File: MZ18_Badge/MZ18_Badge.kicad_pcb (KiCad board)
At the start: 2 copper layers, 76.5 x 89.8 mm, 57 parts, among them CN1 USBMOLEX, IC1 CMWX1ZZABZ-078, IC2 MCP73831_OT, J1 Conn_01x04, J2 Conn_01x04, J3 Conn_01x02, J4 Conn_01x12, J5 U.FL, J6 Conn_01x17, M1 SPI_FLASH-X25XXSMD, Q1 MMBT2222, Q2 MMBT2222, SW1 SW_Push, SW2 SW_Push, U1 ATSAMD21G-A, U2 SPX3819M5-L-3-3, U3 ESP32-WROOM, U4 CP2104, X1 XTALNX5032

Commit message: Desig (almost) done
Via stiching not yet done
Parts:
- removed J4: Conn_01x12, Socket_Strips:Socket_Strip_Angled_2x06_Pitch2.54mm
- removed J6: Conn_01x17, Socket_Strips:Socket_Strip_Angled_1x17_Pitch2.54mm
- added C17: 1u, Capacitors_SMD:C_0603_HandSoldering, B.Cu at (182.0, 130.0)
- added C18: 1u, Capacitors_SMD:C_0603_HandSoldering, B.Cu at (182.0, 127.0)
- added L1: INDUCTOR, Inductors_SMD:L_0603_HandSoldering, B.Cu at (179.0, 128.5)
- added R15: 100k, Resistors_SMD:R_0603_HandSoldering, B.Cu at (162.7, 121.6)
- added R16: 100k, Resistors_SMD:R_0603_HandSoldering, B.Cu at (164.3, 121.6)
- added R17: 0, Resistors_SMD:R_0603_HandSoldering, B.Cu at (128.0, 74.0)
- added R18: 0, Resistors_SMD:R_0603_HandSoldering, B.Cu at (128.0, 72.0)
- added TP1: §, MZ18_Badge:Solderpad, F.Cu at (182.7, 111.5)
- added TP10: §, MZ18_Badge:Solderpad, F.Cu at (182.7, 123.5)
- added TP11: §, MZ18_Badge:Solderpad, B.Cu at (146.5, 67.2)
- added TP12: §, MZ18_Badge:Solderpad, B.Cu at (159.5, 60.5)
- added TP13: §, MZ18_Badge:Solderpad, B.Cu at (169.5, 90.0)
- added TP14: §, MZ18_Badge:Solderpad, B.Cu at (130.0, 118.0)
- added TP15: §, MZ18_Badge:Solderpad, B.Cu at (128.0, 118.0)
- added TP16: §, MZ18_Badge:Solderpad, B.Cu at (126.0, 118.0)
- added TP17: §, MZ18_Badge:Solderpad, B.Cu at (124.0, 118.0)
- added TP18: §, MZ18_Badge:Solderpad, B.Cu at (122.0, 118.0)
- added TP19: §, MZ18_Badge:Solderpad, B.Cu at (120.0, 118.0)
- added TP2: §, MZ18_Badge:Solderpad, F.Cu at (182.7, 113.5)
- added TP20: §, MZ18_Badge:Solderpad, B.Cu at (118.0, 118.0)
- added TP21: §, MZ18_Badge:Solderpad, B.Cu at (133.2, 63.2)
- added TP22: §, MZ18_Badge:Solderpad, B.Cu at (130.8, 63.2)
- added TP23: §, MZ18_Badge:Solderpad, B.Cu at (113.0, 72.0)
- added TP24: §, MZ18_Badge:Solderpad, B.Cu at (163.5, 60.5)
- added TP25: §, MZ18_Badge:Solderpad, B.Cu at (157.4, 118.0)
- added TP26: §, MZ18_Badge:Solderpad, B.Cu at (161.5, 60.5)
- added TP27: §, MZ18_Badge:Solderpad, B.Cu at (145.4, 118.0)
- added TP28: §, MZ18_Badge:Solderpad, B.Cu at (147.4, 118.0)
- added TP29: §, MZ18_Badge:Solderpad, B.Cu at (151.4, 118.0)
- added TP3: §, MZ18_Badge:Solderpad, F.Cu at (182.7, 121.5)
- added TP30: §, MZ18_Badge:Solderpad, B.Cu at (149.4, 118.0)
- added TP31: §, MZ18_Badge:Solderpad, B.Cu at (153.4, 118.0)
- added TP32: §, MZ18_Badge:Solderpad, B.Cu at (155.4, 118.0)
- added TP33: §, MZ18_Badge:Solderpad, B.Cu at (137.4, 118.0)
- added TP34: §, MZ18_Badge:Solderpad, B.Cu at (141.4, 118.0)
- added TP35: §, MZ18_Badge:Solderpad, B.Cu at (139.4, 118.0)
- added TP36: §, MZ18_Badge:Solderpad, B.Cu at (114.0, 118.0)
- added TP37: §, MZ18_Badge:Solderpad, B.Cu at (116.0, 118.0)
- added TP38: §, MZ18_Badge:Solderpad, B.Cu at (112.0, 118.0)
- added TP39: §, MZ18_Badge:Solderpad, B.Cu at (171.5, 90.0)
- added TP4: §, MZ18_Badge:Solderpad, F.Cu at (182.7, 119.5)
- added TP5: §, MZ18_Badge:Solderpad, F.Cu at (182.7, 127.5)
- added TP6: §, MZ18_Badge:Solderpad, F.Cu at (182.7, 129.6)
- added TP7: §, MZ18_Badge:Solderpad, F.Cu at (182.7, 115.5)
- added TP8: §, MZ18_Badge:Solderpad, F.Cu at (182.7, 117.5)
- added TP9: §, MZ18_Badge:Solderpad, F.Cu at (182.7, 125.5)
- CN1: value USBMOLEX -> USBMINIB
- J1: footprint Socket_Strips:Socket_Strip_Angled_1x04_Pitch2.54mm -> Socket_Strips:Socket_Strip_Straight_1x04_Pitch2.54mm
- J2: footprint Socket_Strips:Socket_Strip_Angled_1x04_Pitch2.54mm -> Socket_Strips:Socket_Strip_Straight_2x02_Pitch2.54mm
- R1, R2: value 0R -> 100k
- moved R10 116.9 mm to (98.1, 72.0)
- moved C14 106.2 mm to (108.0, 71.0), turned to 90 degrees
- moved SW2 102.6 mm to (105.0, 67.0), turned to 90 degrees
- moved R12 96.6 mm to (154.9, 69.9), turned to 270 degrees
- moved D8 96.3 mm to (112.5, 102.6)
- moved R13 90.2 mm to (122.7, 91.5), turned to 90 degrees
- moved R14 89.5 mm to (124.7, 91.5), turned to 270 degrees
- moved C16 83.1 mm to (170.4, 80.6)
- moved D2 82.8 mm to (170.5, 68.8), turned to 180 degrees
- moved R9 81.6 mm to (170.7, 72.2), turned to 180 degrees
- moved R7 80.8 mm to (134.8, 68.3)
- moved R8 79.3 mm to (130.6, 68.3)
- moved D7 78.5 mm to (124.0, 102.6)
- moved U3 72.2 mm to (101.5, 85.0), turned to 90 degrees
- moved J1 71.9 mm to (138.4, 59.5)
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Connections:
- CN1 pad 1: (no net) -> VUSB
- CN1 pad 2: (no net) -> D+
- CN1 pad 3: (no net) -> D-
- CN1 pad 5: (no net) -> GND
- CN1 pad 6: (no net) -> GND
- D1 pad 2: (no net) -> VUSB
- IC1 pad 1: Net-(IC1-Pad1) -> (no net)
- IC1 pad 14: (no net) -> /MOSI_LO
- IC1 pad 15: (no net) -> /MISO_LO
- IC1 pad 16: (no net) -> /SCK_LO
- IC1 pad 17: (no net) -> /NSS_LO
- IC1 pad 26: (no net) -> Net-(C18-Pad1)
- IC1 pad 35: (no net) -> /SCL_LO
- IC1 pad 36: (no net) -> /SDA_LO
- IC1 pad 46: (no net) -> Net-(IC1-Pad46)
- IC1 pad 47: (no net) -> Net-(IC1-Pad46)
- IC1 pad 48: VDD_TXCO -> 3V
- J2 pad 1: (no net) -> NRST_LO
- J5 pad 1: (no net) -> Net-(C17-Pad1)
- J5 pad 2: (no net) -> GND
- R1 pad 1: Net-(IC1-Pad1) -> TXD
- R1 pad 2: VDD_TXCO -> 3V
- R2 pad 1: 3V -> RXD
- R2 pad 2: VDD_TXCO -> 3V
- R7 pad 1: A13_I35 -> Net-(R17-Pad2)
- R8 pad 2: A13_I35 -> Net-(R17-Pad2)
- U1 pad 12: A13_I35 -> D9
- U3 pad 10: (no net) -> A1
- U3 pad 11: (no net) -> A0
- U3 pad 12: (no net) -> D11
- U3 pad 13: (no net) -> D5
- U3 pad 14: (no net) -> D12
- U3 pad 16: (no net) -> D13
- U3 pad 23: (no net) -> D9
- U3 pad 26: (no net) -> A5
- U3 pad 27: (no net) -> D0
- U3 pad 28: (no net) -> D1
- U3 pad 4: (no net) -> A4
- U3 pad 5: (no net) -> A3
- U3 pad 6: (no net) -> A2
- U3 pad 8: (no net) -> D6
- U3 pad 9: (no net) -> D10
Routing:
- net 3V: track 71.6 -> 282.6 mm, vias 0 -> 15
- net A4: track 0.00 -> 144.8 mm, vias 0 -> 6
- net A3: track 0.00 -> 139.3 mm, vias 0 -> 6
- net NRESET: track 0.00 -> 137.8 mm, vias 0 -> 6
- net D10: track 0.00 -> 137.8 mm, vias 0 -> 6
- net D6: track 0.00 -> 136.5 mm, vias 0 -> 6
- net D5: track 0.00 -> 135.0 mm, vias 0 -> 8
- net D12: track 0.00 -> 133.7 mm, vias 0 -> 10
- net D11: track 0.00 -> 133.2 mm, vias 0 -> 8
- net A2: track 0.00 -> 131.5 mm, vias 0 -> 6
- net SDA: track 0.00 -> 129.7 mm, vias 0 -> 4
- net A1: track 0.00 -> 127.7 mm, vias 0 -> 6
- net SCK: track 0.00 -> 124.3 mm, vias 0 -> 7
- net SCL: track 0.00 -> 123.7 mm, vias 0 -> 4
- net MISO: track 0.00 -> 120.9 mm, vias 0 -> 6
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- added copper zone on B.Cu, net 3V
- added copper zone on F.Cu, net GND
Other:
- board size 76.5 x 89.8 mm -> 430.6 x 213.9 mm

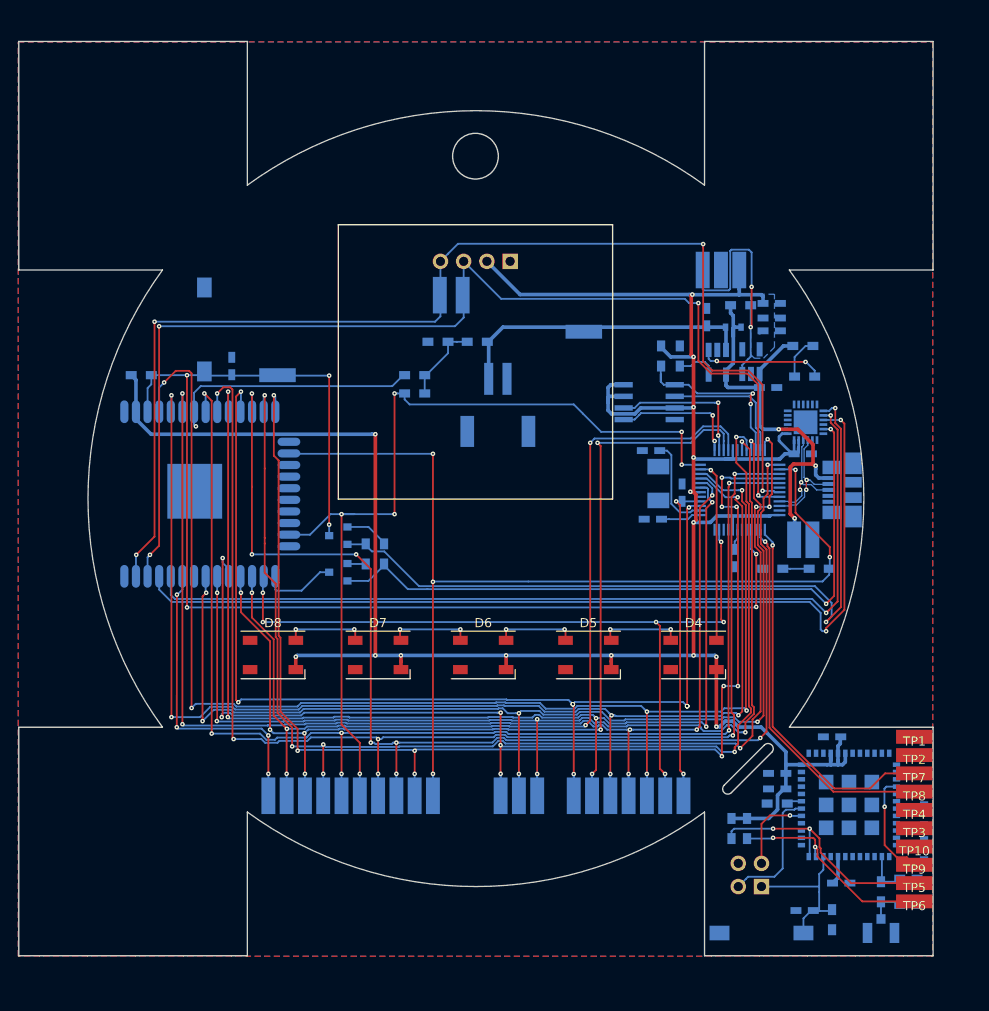
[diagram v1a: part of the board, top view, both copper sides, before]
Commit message: Via stiching and LoRa part
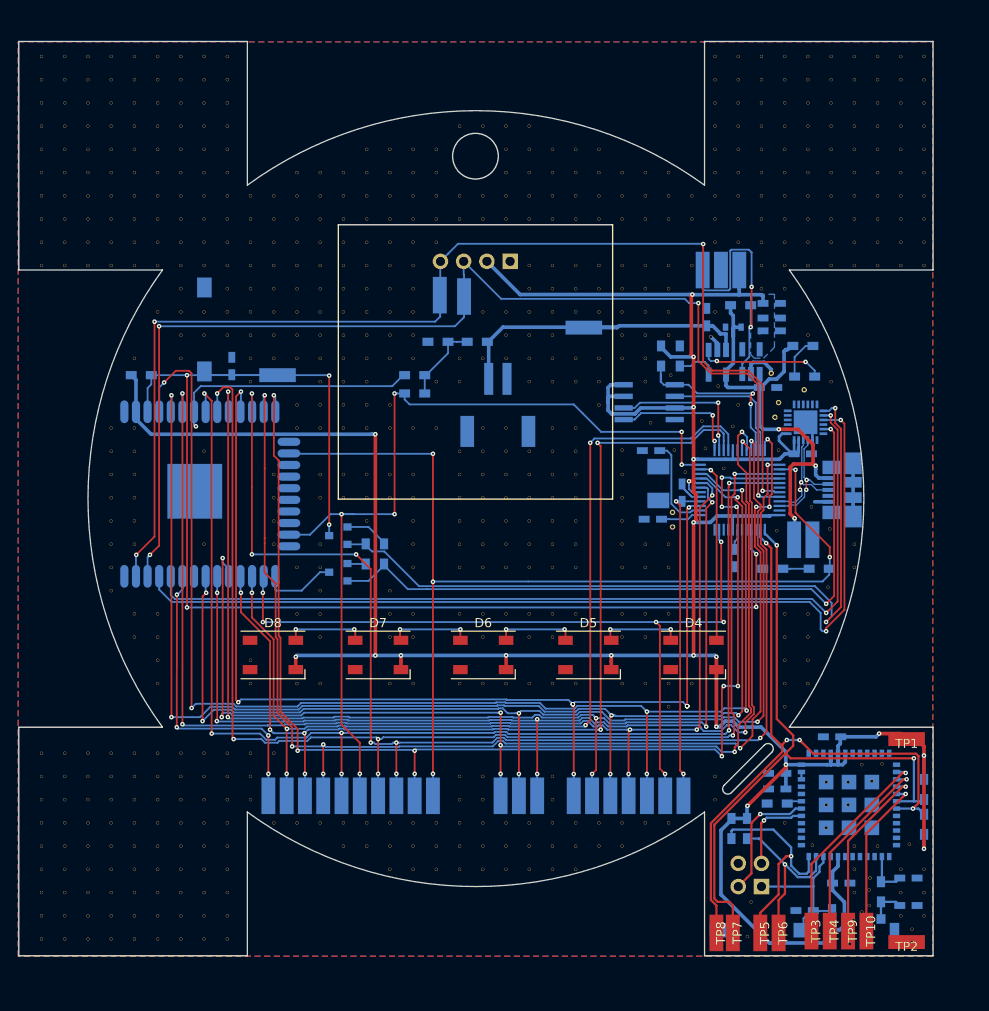
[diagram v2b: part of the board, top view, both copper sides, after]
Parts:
- added REF**: VIA-0.6mm, MZ18_Badge:VIA-0.6mm, F.Cu at (156.2, 88.6)
- added REF**: VIA-0.6mm, MZ18_Badge:VIA-0.6mm, F.Cu at (156.2, 87.0)
- added REF**: VIA-0.6mm, MZ18_Badge:VIA-0.6mm, F.Cu at (170.6, 73.6)
- added REF**: VIA-0.6mm, MZ18_Badge:VIA-0.6mm, F.Cu at (167.8, 75.0)
- added REF**: VIA-0.6mm, MZ18_Badge:VIA-0.6mm, F.Cu at (167.4, 76.6)
- added REF**: VIA-0.6mm, MZ18_Badge:VIA-0.6mm, F.Cu at (167.0, 71.8)
- added V10_17: AUTO_VIA, VIA_MATRIX, F.Cu at (110.0, 52.4)
- added V10_18: AUTO_VIA, VIA_MATRIX, F.Cu at (110.0, 54.9)
- added V10_19: AUTO_VIA, VIA_MATRIX, F.Cu at (110.0, 57.5)
- added V10_20: AUTO_VIA, VIA_MATRIX, F.Cu at (110.0, 60.0)
- added V10_21: AUTO_VIA, VIA_MATRIX, F.Cu at (110.0, 62.5)
- added V10_22: AUTO_VIA, VIA_MATRIX, F.Cu at (110.0, 65.1)
- added V10_23: AUTO_VIA, VIA_MATRIX, F.Cu at (110.0, 67.6)
- added V10_24: AUTO_VIA, VIA_MATRIX, F.Cu at (110.0, 70.2)
- added V10_25: AUTO_VIA, VIA_MATRIX, F.Cu at (110.0, 72.7)
- added V10_37: AUTO_VIA, VIA_MATRIX, F.Cu at (110.0, 103.2)
- added V10_38: AUTO_VIA, VIA_MATRIX, F.Cu at (110.0, 105.7)
- added V10_41: AUTO_VIA, VIA_MATRIX, F.Cu at (110.0, 113.3)
- added V10_42: AUTO_VIA, VIA_MATRIX, F.Cu at (110.0, 115.9)
- added V10_43: AUTO_VIA, VIA_MATRIX, F.Cu at (110.0, 118.4)
- added V11_17: AUTO_VIA, VIA_MATRIX, F.Cu at (112.6, 52.4)
- added V11_18: AUTO_VIA, VIA_MATRIX, F.Cu at (112.6, 54.9)
- added V11_19: AUTO_VIA, VIA_MATRIX, F.Cu at (112.6, 57.5)
- added V11_20: AUTO_VIA, VIA_MATRIX, F.Cu at (112.6, 60.0)
- added V11_21: AUTO_VIA, VIA_MATRIX, F.Cu at (112.6, 62.5)
- added V11_22: AUTO_VIA, VIA_MATRIX, F.Cu at (112.6, 65.1)
- added V11_23: AUTO_VIA, VIA_MATRIX, F.Cu at (112.6, 67.6)
- added V11_24: AUTO_VIA, VIA_MATRIX, F.Cu at (112.6, 70.2)
- added V11_29: AUTO_VIA, VIA_MATRIX, F.Cu at (112.6, 82.9)
- added V11_30: AUTO_VIA, VIA_MATRIX, F.Cu at (112.6, 85.4)
- added V11_31: AUTO_VIA, VIA_MATRIX, F.Cu at (112.6, 87.9)
- added V11_32: AUTO_VIA, VIA_MATRIX, F.Cu at (112.6, 90.5)
- added V11_41: AUTO_VIA, VIA_MATRIX, F.Cu at (112.6, 113.3)
- added V11_44: AUTO_VIA, VIA_MATRIX, F.Cu at (112.6, 121.0)
- added V12_16: AUTO_VIA, VIA_MATRIX, F.Cu at (115.1, 49.8)
- added V12_17: AUTO_VIA, VIA_MATRIX, F.Cu at (115.1, 52.4)
- added V12_18: AUTO_VIA, VIA_MATRIX, F.Cu at (115.1, 54.9)
- added V12_19: AUTO_VIA, VIA_MATRIX, F.Cu at (115.1, 57.5)
- added V12_20: AUTO_VIA, VIA_MATRIX, F.Cu at (115.1, 60.0)
- added V12_21: AUTO_VIA, VIA_MATRIX, F.Cu at (115.1, 62.5)
- added V12_22: AUTO_VIA, VIA_MATRIX, F.Cu at (115.1, 65.1)
- added V12_23: AUTO_VIA, VIA_MATRIX, F.Cu at (115.1, 67.6)
- added V12_24: AUTO_VIA, VIA_MATRIX, F.Cu at (115.1, 70.2)
- added V12_26: AUTO_VIA, VIA_MATRIX, F.Cu at (115.1, 75.2)
- added V12_27: AUTO_VIA, VIA_MATRIX, F.Cu at (115.1, 77.8)
- added V12_33: AUTO_VIA, VIA_MATRIX, F.Cu at (115.1, 93.0)
- added V12_35: AUTO_VIA, VIA_MATRIX, F.Cu at (115.1, 98.1)
- added V12_38: AUTO_VIA, VIA_MATRIX, F.Cu at (115.1, 105.7)
- added V12_44: AUTO_VIA, VIA_MATRIX, F.Cu at (115.1, 121.0)
- added V13_16: AUTO_VIA, VIA_MATRIX, F.Cu at (117.7, 49.8)
- added V13_17: AUTO_VIA, VIA_MATRIX, F.Cu at (117.7, 52.4)
- added V13_18: AUTO_VIA, VIA_MATRIX, F.Cu at (117.7, 54.9)
- added V13_19: AUTO_VIA, VIA_MATRIX, F.Cu at (117.7, 57.5)
- added V13_20: AUTO_VIA, VIA_MATRIX, F.Cu at (117.7, 60.0)
- added V13_21: AUTO_VIA, VIA_MATRIX, F.Cu at (117.7, 62.5)
- added V13_22: AUTO_VIA, VIA_MATRIX, F.Cu at (117.7, 65.1)
- added V13_23: AUTO_VIA, VIA_MATRIX, F.Cu at (117.7, 67.6)
- added V13_24: AUTO_VIA, VIA_MATRIX, F.Cu at (117.7, 70.2)
- added V13_25: AUTO_VIA, VIA_MATRIX, F.Cu at (117.7, 72.7)
- added V13_26: AUTO_VIA, VIA_MATRIX, F.Cu at (117.7, 75.2)
- added V13_27: AUTO_VIA, VIA_MATRIX, F.Cu at (117.7, 77.8)
- added V13_29: AUTO_VIA, VIA_MATRIX, F.Cu at (117.7, 82.9)
- added V13_30: AUTO_VIA, VIA_MATRIX, F.Cu at (117.7, 85.4)
- added V13_32: AUTO_VIA, VIA_MATRIX, F.Cu at (117.7, 90.5)
- added V13_33: AUTO_VIA, VIA_MATRIX, F.Cu at (117.7, 93.0)
- added V13_34: AUTO_VIA, VIA_MATRIX, F.Cu at (117.7, 95.6)
- added V13_35: AUTO_VIA, VIA_MATRIX, F.Cu at (117.7, 98.1)
- added V13_36: AUTO_VIA, VIA_MATRIX, F.Cu at (117.7, 100.6)
- added V13_38: AUTO_VIA, VIA_MATRIX, F.Cu at (117.7, 105.7)
- added V13_44: AUTO_VIA, VIA_MATRIX, F.Cu at (117.7, 121.0)
- added V14_16: AUTO_VIA, VIA_MATRIX, F.Cu at (120.2, 49.8)
- added V14_17: AUTO_VIA, VIA_MATRIX, F.Cu at (120.2, 52.4)
- added V14_18: AUTO_VIA, VIA_MATRIX, F.Cu at (120.2, 54.9)
- added V14_19: AUTO_VIA, VIA_MATRIX, F.Cu at (120.2, 57.5)
- added V14_20: AUTO_VIA, VIA_MATRIX, F.Cu at (120.2, 60.0)
- added V14_21: AUTO_VIA, VIA_MATRIX, F.Cu at (120.2, 62.5)
- added V14_22: AUTO_VIA, VIA_MATRIX, F.Cu at (120.2, 65.1)
- added V14_23: AUTO_VIA, VIA_MATRIX, F.Cu at (120.2, 67.6)
- added V14_24: AUTO_VIA, VIA_MATRIX, F.Cu at (120.2, 70.2)
- added V14_25: AUTO_VIA, VIA_MATRIX, F.Cu at (120.2, 72.7)
- added V14_26: AUTO_VIA, VIA_MATRIX, F.Cu at (120.2, 75.2)
- added V14_27: AUTO_VIA, VIA_MATRIX, F.Cu at (120.2, 77.8)
- added V14_29: AUTO_VIA, VIA_MATRIX, F.Cu at (120.2, 82.9)
- added V14_30: AUTO_VIA, VIA_MATRIX, F.Cu at (120.2, 85.4)
- added V14_44: AUTO_VIA, VIA_MATRIX, F.Cu at (120.2, 121.0)
- added V14_45: AUTO_VIA, VIA_MATRIX, F.Cu at (120.2, 123.5)
- added V15_15: AUTO_VIA, VIA_MATRIX, F.Cu at (122.7, 47.3)
- added V15_16: AUTO_VIA, VIA_MATRIX, F.Cu at (122.7, 49.8)
- added V15_17: AUTO_VIA, VIA_MATRIX, F.Cu at (122.7, 52.4)
- added V15_18: AUTO_VIA, VIA_MATRIX, F.Cu at (122.7, 54.9)
- added V15_19: AUTO_VIA, VIA_MATRIX, F.Cu at (122.7, 57.5)
- added V15_20: AUTO_VIA, VIA_MATRIX, F.Cu at (122.7, 60.0)
- added V15_21: AUTO_VIA, VIA_MATRIX, F.Cu at (122.7, 62.5)
- added V15_22: AUTO_VIA, VIA_MATRIX, F.Cu at (122.7, 65.1)
- added V15_23: AUTO_VIA, VIA_MATRIX, F.Cu at (122.7, 67.6)
- added V15_24: AUTO_VIA, VIA_MATRIX, F.Cu at (122.7, 70.2)
- added V15_25: AUTO_VIA, VIA_MATRIX, F.Cu at (122.7, 72.7)
- added V15_26: AUTO_VIA, VIA_MATRIX, F.Cu at (122.7, 75.2)
- added V15_27: AUTO_VIA, VIA_MATRIX, F.Cu at (122.7, 77.8)
- added V15_29: AUTO_VIA, VIA_MATRIX, F.Cu at (122.7, 82.9)
- added V15_30: AUTO_VIA, VIA_MATRIX, F.Cu at (122.7, 85.4)
- added V15_31: AUTO_VIA, VIA_MATRIX, F.Cu at (122.7, 87.9)
- added V15_44: AUTO_VIA, VIA_MATRIX, F.Cu at (122.7, 121.0)
- added V15_45: AUTO_VIA, VIA_MATRIX, F.Cu at (122.7, 123.5)
- added V16_15: AUTO_VIA, VIA_MATRIX, F.Cu at (125.3, 47.3)
- added V16_16: AUTO_VIA, VIA_MATRIX, F.Cu at (125.3, 49.8)
- added V16_17: AUTO_VIA, VIA_MATRIX, F.Cu at (125.3, 52.4)
- added V16_18: AUTO_VIA, VIA_MATRIX, F.Cu at (125.3, 54.9)
- added V16_19: AUTO_VIA, VIA_MATRIX, F.Cu at (125.3, 57.5)
- added V16_20: AUTO_VIA, VIA_MATRIX, F.Cu at (125.3, 60.0)
- added V16_21: AUTO_VIA, VIA_MATRIX, F.Cu at (125.3, 62.5)
- added V16_22: AUTO_VIA, VIA_MATRIX, F.Cu at (125.3, 65.1)
- added V16_23: AUTO_VIA, VIA_MATRIX, F.Cu at (125.3, 67.6)
- added V16_24: AUTO_VIA, VIA_MATRIX, F.Cu at (125.3, 70.2)
- added V16_26: AUTO_VIA, VIA_MATRIX, F.Cu at (125.3, 75.2)
- added V16_27: AUTO_VIA, VIA_MATRIX, F.Cu at (125.3, 77.8)
- added V16_29: AUTO_VIA, VIA_MATRIX, F.Cu at (125.3, 82.9)
- added V16_30: AUTO_VIA, VIA_MATRIX, F.Cu at (125.3, 85.4)
- added V16_34: AUTO_VIA, VIA_MATRIX, F.Cu at (125.3, 95.6)
- added V16_35: AUTO_VIA, VIA_MATRIX, F.Cu at (125.3, 98.1)
- added V16_36: AUTO_VIA, VIA_MATRIX, F.Cu at (125.3, 100.6)
- added V16_38: AUTO_VIA, VIA_MATRIX, F.Cu at (125.3, 105.7)
- added V16_44: AUTO_VIA, VIA_MATRIX, F.Cu at (125.3, 121.0)
- added V16_45: AUTO_VIA, VIA_MATRIX, F.Cu at (125.3, 123.5)
- added V16_46: AUTO_VIA, VIA_MATRIX, F.Cu at (125.3, 126.0)
- added V17_15: AUTO_VIA, VIA_MATRIX, F.Cu at (127.8, 47.3)
- added V17_16: AUTO_VIA, VIA_MATRIX, F.Cu at (127.8, 49.8)
- added V17_17: AUTO_VIA, VIA_MATRIX, F.Cu at (127.8, 52.4)
- added V17_18: AUTO_VIA, VIA_MATRIX, F.Cu at (127.8, 54.9)
- added V17_19: AUTO_VIA, VIA_MATRIX, F.Cu at (127.8, 57.5)
- added V17_20: AUTO_VIA, VIA_MATRIX, F.Cu at (127.8, 60.0)
- added V17_21: AUTO_VIA, VIA_MATRIX, F.Cu at (127.8, 62.5)
- added V17_22: AUTO_VIA, VIA_MATRIX, F.Cu at (127.8, 65.1)
- added V17_23: AUTO_VIA, VIA_MATRIX, F.Cu at (127.8, 67.6)
- added V17_24: AUTO_VIA, VIA_MATRIX, F.Cu at (127.8, 70.2)
- added V17_27: AUTO_VIA, VIA_MATRIX, F.Cu at (127.8, 77.8)
- added V17_29: AUTO_VIA, VIA_MATRIX, F.Cu at (127.8, 82.9)
- added V17_30: AUTO_VIA, VIA_MATRIX, F.Cu at (127.8, 85.4)
- added V17_31: AUTO_VIA, VIA_MATRIX, F.Cu at (127.8, 87.9)
- added V17_32: AUTO_VIA, VIA_MATRIX, F.Cu at (127.8, 90.5)
- added V17_33: AUTO_VIA, VIA_MATRIX, F.Cu at (127.8, 93.0)
- added V17_35: AUTO_VIA, VIA_MATRIX, F.Cu at (127.8, 98.1)
- added V17_36: AUTO_VIA, VIA_MATRIX, F.Cu at (127.8, 100.6)
- added V17_38: AUTO_VIA, VIA_MATRIX, F.Cu at (127.8, 105.7)
- added V17_44: AUTO_VIA, VIA_MATRIX, F.Cu at (127.8, 121.0)
- added V17_45: AUTO_VIA, VIA_MATRIX, F.Cu at (127.8, 123.5)
- added V17_46: AUTO_VIA, VIA_MATRIX, F.Cu at (127.8, 126.0)
- added V18_15: AUTO_VIA, VIA_MATRIX, F.Cu at (130.4, 47.3)
- added V18_16: AUTO_VIA, VIA_MATRIX, F.Cu at (130.4, 49.8)
- added V18_17: AUTO_VIA, VIA_MATRIX, F.Cu at (130.4, 52.4)
- added V18_18: AUTO_VIA, VIA_MATRIX, F.Cu at (130.4, 54.9)
- added V18_19: AUTO_VIA, VIA_MATRIX, F.Cu at (130.4, 57.5)
- added V18_25: AUTO_VIA, VIA_MATRIX, F.Cu at (130.4, 72.7)
- added V18_27: AUTO_VIA, VIA_MATRIX, F.Cu at (130.4, 77.8)
- added V18_44: AUTO_VIA, VIA_MATRIX, F.Cu at (130.4, 121.0)
- added V18_45: AUTO_VIA, VIA_MATRIX, F.Cu at (130.4, 123.5)
- added V18_46: AUTO_VIA, VIA_MATRIX, F.Cu at (130.4, 126.0)
- added V19_14: AUTO_VIA, VIA_MATRIX, F.Cu at (132.9, 44.8)
- added V19_17: AUTO_VIA, VIA_MATRIX, F.Cu at (132.9, 52.4)
- added V19_18: AUTO_VIA, VIA_MATRIX, F.Cu at (132.9, 54.9)
- added V19_24: AUTO_VIA, VIA_MATRIX, F.Cu at (132.9, 70.2)
- added V19_25: AUTO_VIA, VIA_MATRIX, F.Cu at (132.9, 72.7)
- added V19_28: AUTO_VIA, VIA_MATRIX, F.Cu at (132.9, 80.3)
- added V19_29: AUTO_VIA, VIA_MATRIX, F.Cu at (132.9, 82.9)
- added V19_30: AUTO_VIA, VIA_MATRIX, F.Cu at (132.9, 85.4)
- added V19_31: AUTO_VIA, VIA_MATRIX, F.Cu at (132.9, 87.9)
- added V19_32: AUTO_VIA, VIA_MATRIX, F.Cu at (132.9, 90.5)
- added V19_33: AUTO_VIA, VIA_MATRIX, F.Cu at (132.9, 93.0)
- added V19_35: AUTO_VIA, VIA_MATRIX, F.Cu at (132.9, 98.1)
- added V19_38: AUTO_VIA, VIA_MATRIX, F.Cu at (132.9, 105.7)
- added V19_42: AUTO_VIA, VIA_MATRIX, F.Cu at (132.9, 115.9)
- added V19_43: AUTO_VIA, VIA_MATRIX, F.Cu at (132.9, 118.4)
- added V19_44: AUTO_VIA, VIA_MATRIX, F.Cu at (132.9, 121.0)
- added V19_45: AUTO_VIA, VIA_MATRIX, F.Cu at (132.9, 123.5)
- added V19_46: AUTO_VIA, VIA_MATRIX, F.Cu at (132.9, 126.0)
- added V1_11: AUTO_VIA, VIA_MATRIX, F.Cu at (87.2, 37.1)
- added V1_12: AUTO_VIA, VIA_MATRIX, F.Cu at (87.2, 39.7)
- added V1_13: AUTO_VIA, VIA_MATRIX, F.Cu at (87.2, 42.2)
- added V1_14: AUTO_VIA, VIA_MATRIX, F.Cu at (87.2, 44.8)
- added V1_15: AUTO_VIA, VIA_MATRIX, F.Cu at (87.2, 47.3)
- added V1_16: AUTO_VIA, VIA_MATRIX, F.Cu at (87.2, 49.8)
- added V1_17: AUTO_VIA, VIA_MATRIX, F.Cu at (87.2, 52.4)
- added V1_18: AUTO_VIA, VIA_MATRIX, F.Cu at (87.2, 54.9)
- added V1_19: AUTO_VIA, VIA_MATRIX, F.Cu at (87.2, 57.5)
- added V1_20: AUTO_VIA, VIA_MATRIX, F.Cu at (87.2, 60.0)
- added V1_41: AUTO_VIA, VIA_MATRIX, F.Cu at (87.2, 113.3)
- added V1_42: AUTO_VIA, VIA_MATRIX, F.Cu at (87.2, 115.9)
- added V1_43: AUTO_VIA, VIA_MATRIX, F.Cu at (87.2, 118.4)
- added V1_44: AUTO_VIA, VIA_MATRIX, F.Cu at (87.2, 121.0)
- added V1_45: AUTO_VIA, VIA_MATRIX, F.Cu at (87.2, 123.5)
- added V1_46: AUTO_VIA, VIA_MATRIX, F.Cu at (87.2, 126.0)
- added V1_47: AUTO_VIA, VIA_MATRIX, F.Cu at (87.2, 128.6)
- added V1_48: AUTO_VIA, VIA_MATRIX, F.Cu at (87.2, 131.1)
- added V1_49: AUTO_VIA, VIA_MATRIX, F.Cu at (87.2, 133.7)
- added V20_14: AUTO_VIA, VIA_MATRIX, F.Cu at (135.4, 44.8)
- added V20_17: AUTO_VIA, VIA_MATRIX, F.Cu at (135.4, 52.4)
- added V20_18: AUTO_VIA, VIA_MATRIX, F.Cu at (135.4, 54.9)
- added V20_22: AUTO_VIA, VIA_MATRIX, F.Cu at (135.4, 65.1)
- added V20_24: AUTO_VIA, VIA_MATRIX, F.Cu at (135.4, 70.2)
- added V20_27: AUTO_VIA, VIA_MATRIX, F.Cu at (135.4, 77.8)
- added V20_28: AUTO_VIA, VIA_MATRIX, F.Cu at (135.4, 80.3)
- added V20_29: AUTO_VIA, VIA_MATRIX, F.Cu at (135.4, 82.9)
- added V20_30: AUTO_VIA, VIA_MATRIX, F.Cu at (135.4, 85.4)
- added V20_31: AUTO_VIA, VIA_MATRIX, F.Cu at (135.4, 87.9)
- added V20_32: AUTO_VIA, VIA_MATRIX, F.Cu at (135.4, 90.5)
- added V20_33: AUTO_VIA, VIA_MATRIX, F.Cu at (135.4, 93.0)
- added V20_35: AUTO_VIA, VIA_MATRIX, F.Cu at (135.4, 98.1)
- added V20_36: AUTO_VIA, VIA_MATRIX, F.Cu at (135.4, 100.6)
- added V20_38: AUTO_VIA, VIA_MATRIX, F.Cu at (135.4, 105.7)
- added V20_42: AUTO_VIA, VIA_MATRIX, F.Cu at (135.4, 115.9)
- added V20_43: AUTO_VIA, VIA_MATRIX, F.Cu at (135.4, 118.4)
- added V20_44: AUTO_VIA, VIA_MATRIX, F.Cu at (135.4, 121.0)
- added V20_45: AUTO_VIA, VIA_MATRIX, F.Cu at (135.4, 123.5)
- added V20_46: AUTO_VIA, VIA_MATRIX, F.Cu at (135.4, 126.0)
- added V21_14: AUTO_VIA, VIA_MATRIX, F.Cu at (138.0, 44.8)
- added V21_15: AUTO_VIA, VIA_MATRIX, F.Cu at (138.0, 47.3)
- added V21_16: AUTO_VIA, VIA_MATRIX, F.Cu at (138.0, 49.8)
- added V21_17: AUTO_VIA, VIA_MATRIX, F.Cu at (138.0, 52.4)
- added V21_18: AUTO_VIA, VIA_MATRIX, F.Cu at (138.0, 54.9)
- added V21_22: AUTO_VIA, VIA_MATRIX, F.Cu at (138.0, 65.1)
- added V21_23: AUTO_VIA, VIA_MATRIX, F.Cu at (138.0, 67.6)
- added V21_24: AUTO_VIA, VIA_MATRIX, F.Cu at (138.0, 70.2)
- added V21_27: AUTO_VIA, VIA_MATRIX, F.Cu at (138.0, 77.8)
- added V21_28: AUTO_VIA, VIA_MATRIX, F.Cu at (138.0, 80.3)
- added V21_29: AUTO_VIA, VIA_MATRIX, F.Cu at (138.0, 82.9)
- added V21_30: AUTO_VIA, VIA_MATRIX, F.Cu at (138.0, 85.4)
- added V21_31: AUTO_VIA, VIA_MATRIX, F.Cu at (138.0, 87.9)
- added V21_32: AUTO_VIA, VIA_MATRIX, F.Cu at (138.0, 90.5)
- added V21_33: AUTO_VIA, VIA_MATRIX, F.Cu at (138.0, 93.0)
- added V21_35: AUTO_VIA, VIA_MATRIX, F.Cu at (138.0, 98.1)
- added V21_38: AUTO_VIA, VIA_MATRIX, F.Cu at (138.0, 105.7)
- added V21_44: AUTO_VIA, VIA_MATRIX, F.Cu at (138.0, 121.0)
- added V21_45: AUTO_VIA, VIA_MATRIX, F.Cu at (138.0, 123.5)
- added V21_46: AUTO_VIA, VIA_MATRIX, F.Cu at (138.0, 126.0)
- added V22_14: AUTO_VIA, VIA_MATRIX, F.Cu at (140.5, 44.8)
- added V22_15: AUTO_VIA, VIA_MATRIX, F.Cu at (140.5, 47.3)
- added V22_16: AUTO_VIA, VIA_MATRIX, F.Cu at (140.5, 49.8)
- added V22_17: AUTO_VIA, VIA_MATRIX, F.Cu at (140.5, 52.4)
- added V22_18: AUTO_VIA, VIA_MATRIX, F.Cu at (140.5, 54.9)
- added V22_20: AUTO_VIA, VIA_MATRIX, F.Cu at (140.5, 60.0)
- added V22_21: AUTO_VIA, VIA_MATRIX, F.Cu at (140.5, 62.5)
- added V22_22: AUTO_VIA, VIA_MATRIX, F.Cu at (140.5, 65.1)
- added V22_23: AUTO_VIA, VIA_MATRIX, F.Cu at (140.5, 67.6)
- added V22_24: AUTO_VIA, VIA_MATRIX, F.Cu at (140.5, 70.2)
- added V22_25: AUTO_VIA, VIA_MATRIX, F.Cu at (140.5, 72.7)
- added V22_28: AUTO_VIA, VIA_MATRIX, F.Cu at (140.5, 80.3)
- added V22_29: AUTO_VIA, VIA_MATRIX, F.Cu at (140.5, 82.9)
- added V22_30: AUTO_VIA, VIA_MATRIX, F.Cu at (140.5, 85.4)
- added V22_31: AUTO_VIA, VIA_MATRIX, F.Cu at (140.5, 87.9)
- added V22_32: AUTO_VIA, VIA_MATRIX, F.Cu at (140.5, 90.5)
- added V22_33: AUTO_VIA, VIA_MATRIX, F.Cu at (140.5, 93.0)
- added V22_35: AUTO_VIA, VIA_MATRIX, F.Cu at (140.5, 98.1)
- added V22_36: AUTO_VIA, VIA_MATRIX, F.Cu at (140.5, 100.6)
- added V22_38: AUTO_VIA, VIA_MATRIX, F.Cu at (140.5, 105.7)
- added V22_44: AUTO_VIA, VIA_MATRIX, F.Cu at (140.5, 121.0)
- added V22_45: AUTO_VIA, VIA_MATRIX, F.Cu at (140.5, 123.5)
- added V22_46: AUTO_VIA, VIA_MATRIX, F.Cu at (140.5, 126.0)
- added V23_15: AUTO_VIA, VIA_MATRIX, F.Cu at (143.1, 47.3)
- added V23_16: AUTO_VIA, VIA_MATRIX, F.Cu at (143.1, 49.8)
- added V23_17: AUTO_VIA, VIA_MATRIX, F.Cu at (143.1, 52.4)
- added V23_18: AUTO_VIA, VIA_MATRIX, F.Cu at (143.1, 54.9)
- added V23_20: AUTO_VIA, VIA_MATRIX, F.Cu at (143.1, 60.0)
- added V23_21: AUTO_VIA, VIA_MATRIX, F.Cu at (143.1, 62.5)
- added V23_22: AUTO_VIA, VIA_MATRIX, F.Cu at (143.1, 65.1)
- added V23_23: AUTO_VIA, VIA_MATRIX, F.Cu at (143.1, 67.6)
- added V23_24: AUTO_VIA, VIA_MATRIX, F.Cu at (143.1, 70.2)
- added V23_25: AUTO_VIA, VIA_MATRIX, F.Cu at (143.1, 72.7)
- added V23_27: AUTO_VIA, VIA_MATRIX, F.Cu at (143.1, 77.8)
- added V23_28: AUTO_VIA, VIA_MATRIX, F.Cu at (143.1, 80.3)
- added V23_29: AUTO_VIA, VIA_MATRIX, F.Cu at (143.1, 82.9)
- added V23_30: AUTO_VIA, VIA_MATRIX, F.Cu at (143.1, 85.4)
- added V23_31: AUTO_VIA, VIA_MATRIX, F.Cu at (143.1, 87.9)
- added V23_32: AUTO_VIA, VIA_MATRIX, F.Cu at (143.1, 90.5)
- added V23_33: AUTO_VIA, VIA_MATRIX, F.Cu at (143.1, 93.0)
- added V23_35: AUTO_VIA, VIA_MATRIX, F.Cu at (143.1, 98.1)
- added V23_36: AUTO_VIA, VIA_MATRIX, F.Cu at (143.1, 100.6)
- added V23_38: AUTO_VIA, VIA_MATRIX, F.Cu at (143.1, 105.7)
- added V23_42: AUTO_VIA, VIA_MATRIX, F.Cu at (143.1, 115.9)
- added V23_43: AUTO_VIA, VIA_MATRIX, F.Cu at (143.1, 118.4)
- added V23_44: AUTO_VIA, VIA_MATRIX, F.Cu at (143.1, 121.0)
- added V23_45: AUTO_VIA, VIA_MATRIX, F.Cu at (143.1, 123.5)
- added V23_46: AUTO_VIA, VIA_MATRIX, F.Cu at (143.1, 126.0)
- added V24_15: AUTO_VIA, VIA_MATRIX, F.Cu at (145.6, 47.3)
- added V24_16: AUTO_VIA, VIA_MATRIX, F.Cu at (145.6, 49.8)
- added V24_17: AUTO_VIA, VIA_MATRIX, F.Cu at (145.6, 52.4)
- added V24_18: AUTO_VIA, VIA_MATRIX, F.Cu at (145.6, 54.9)
- added V24_20: AUTO_VIA, VIA_MATRIX, F.Cu at (145.6, 60.0)
- added V24_21: AUTO_VIA, VIA_MATRIX, F.Cu at (145.6, 62.5)
- added V24_22: AUTO_VIA, VIA_MATRIX, F.Cu at (145.6, 65.1)
- added V24_24: AUTO_VIA, VIA_MATRIX, F.Cu at (145.6, 70.2)
- added V24_25: AUTO_VIA, VIA_MATRIX, F.Cu at (145.6, 72.7)
- added V24_27: AUTO_VIA, VIA_MATRIX, F.Cu at (145.6, 77.8)
- added V24_28: AUTO_VIA, VIA_MATRIX, F.Cu at (145.6, 80.3)
- added V24_29: AUTO_VIA, VIA_MATRIX, F.Cu at (145.6, 82.9)
- added V24_30: AUTO_VIA, VIA_MATRIX, F.Cu at (145.6, 85.4)
- added V24_31: AUTO_VIA, VIA_MATRIX, F.Cu at (145.6, 87.9)
- added V24_32: AUTO_VIA, VIA_MATRIX, F.Cu at (145.6, 90.5)
- added V24_33: AUTO_VIA, VIA_MATRIX, F.Cu at (145.6, 93.0)
- added V24_35: AUTO_VIA, VIA_MATRIX, F.Cu at (145.6, 98.1)
- added V24_38: AUTO_VIA, VIA_MATRIX, F.Cu at (145.6, 105.7)
- added V24_44: AUTO_VIA, VIA_MATRIX, F.Cu at (145.6, 121.0)
- added V24_45: AUTO_VIA, VIA_MATRIX, F.Cu at (145.6, 123.5)
- added V24_46: AUTO_VIA, VIA_MATRIX, F.Cu at (145.6, 126.0)
- added V25_15: AUTO_VIA, VIA_MATRIX, F.Cu at (148.1, 47.3)
- added V25_16: AUTO_VIA, VIA_MATRIX, F.Cu at (148.1, 49.8)
- added V25_17: AUTO_VIA, VIA_MATRIX, F.Cu at (148.1, 52.4)
- added V25_18: AUTO_VIA, VIA_MATRIX, F.Cu at (148.1, 54.9)
- added V25_20: AUTO_VIA, VIA_MATRIX, F.Cu at (148.1, 60.0)
- added V25_21: AUTO_VIA, VIA_MATRIX, F.Cu at (148.1, 62.5)
- added V25_22: AUTO_VIA, VIA_MATRIX, F.Cu at (148.1, 65.1)
- added V25_24: AUTO_VIA, VIA_MATRIX, F.Cu at (148.1, 70.2)
- added V25_25: AUTO_VIA, VIA_MATRIX, F.Cu at (148.1, 72.7)
- added V25_26: AUTO_VIA, VIA_MATRIX, F.Cu at (148.1, 75.2)
- added V25_44: AUTO_VIA, VIA_MATRIX, F.Cu at (148.1, 121.0)
- added V25_45: AUTO_VIA, VIA_MATRIX, F.Cu at (148.1, 123.5)
- added V26_16: AUTO_VIA, VIA_MATRIX, F.Cu at (150.7, 49.8)
- added V26_17: AUTO_VIA, VIA_MATRIX, F.Cu at (150.7, 52.4)
- added V26_18: AUTO_VIA, VIA_MATRIX, F.Cu at (150.7, 54.9)
- added V26_20: AUTO_VIA, VIA_MATRIX, F.Cu at (150.7, 60.0)
- added V26_21: AUTO_VIA, VIA_MATRIX, F.Cu at (150.7, 62.5)
- added V26_22: AUTO_VIA, VIA_MATRIX, F.Cu at (150.7, 65.1)
- added V26_23: AUTO_VIA, VIA_MATRIX, F.Cu at (150.7, 67.6)
- added V26_24: AUTO_VIA, VIA_MATRIX, F.Cu at (150.7, 70.2)
- added V26_29: AUTO_VIA, VIA_MATRIX, F.Cu at (159.4, 77.0)
- added V26_29: AUTO_VIA, VIA_MATRIX, F.Cu at (153.8, 77.2)
- added V26_29: AUTO_VIA, VIA_MATRIX, F.Cu at (159.8, 80.0)
- added V26_29: AUTO_VIA, VIA_MATRIX, F.Cu at (150.7, 80.2)
- added V26_29: AUTO_VIA, VIA_MATRIX, F.Cu at (150.7, 82.9)
- added V26_29: AUTO_VIA, VIA_MATRIX, F.Cu at (156.4, 80.2)
- added V26_29: AUTO_VIA, VIA_MATRIX, F.Cu at (157.6, 82.6)
- added V26_29: AUTO_VIA, VIA_MATRIX, F.Cu at (161.8, 82.2)
- added V26_29: AUTO_VIA, VIA_MATRIX, F.Cu at (171.4, 86.4)
- added V26_29: AUTO_VIA, VIA_MATRIX, F.Cu at (173.4, 88.8)
- added V26_29: AUTO_VIA, VIA_MATRIX, F.Cu at (167.6, 89.0)
- added V26_29: AUTO_VIA, VIA_MATRIX, F.Cu at (167.8, 80.2)
- added V26_29: AUTO_VIA, VIA_MATRIX, F.Cu at (162.8, 77.6)
- added V26_30: AUTO_VIA, VIA_MATRIX, F.Cu at (150.7, 85.4)
- added V26_31: AUTO_VIA, VIA_MATRIX, F.Cu at (150.7, 87.9)
- added V26_32: AUTO_VIA, VIA_MATRIX, F.Cu at (150.7, 90.5)
- added V26_33: AUTO_VIA, VIA_MATRIX, F.Cu at (150.7, 93.0)
- added V26_35: AUTO_VIA, VIA_MATRIX, F.Cu at (150.7, 98.1)
- added V26_36: AUTO_VIA, VIA_MATRIX, F.Cu at (150.7, 100.6)
- added V26_38: AUTO_VIA, VIA_MATRIX, F.Cu at (150.7, 105.7)
- added V26_44: AUTO_VIA, VIA_MATRIX, F.Cu at (150.7, 121.0)
- added V26_45: AUTO_VIA, VIA_MATRIX, F.Cu at (150.7, 123.5)
- added V27_16: AUTO_VIA, VIA_MATRIX, F.Cu at (153.2, 49.8)
- added V27_17: AUTO_VIA, VIA_MATRIX, F.Cu at (153.2, 52.4)
- added V27_18: AUTO_VIA, VIA_MATRIX, F.Cu at (153.2, 54.9)
- added V27_20: AUTO_VIA, VIA_MATRIX, F.Cu at (153.2, 60.0)
- added V27_21: AUTO_VIA, VIA_MATRIX, F.Cu at (153.2, 62.5)
- added V27_22: AUTO_VIA, VIA_MATRIX, F.Cu at (153.2, 65.1)
- added V27_23: AUTO_VIA, VIA_MATRIX, F.Cu at (153.2, 67.6)
- added V27_24: AUTO_VIA, VIA_MATRIX, F.Cu at (153.2, 70.2)
- added V27_25: AUTO_VIA, VIA_MATRIX, F.Cu at (161.2, 73.2)
- added V27_25: AUTO_VIA, VIA_MATRIX, F.Cu at (156.0, 72.0)
- added V27_25: AUTO_VIA, VIA_MATRIX, F.Cu at (153.2, 72.7)
- added V27_32: AUTO_VIA, VIA_MATRIX, F.Cu at (153.2, 90.5)
- added V27_33: AUTO_VIA, VIA_MATRIX, F.Cu at (153.2, 93.0)
- added V27_35: AUTO_VIA, VIA_MATRIX, F.Cu at (153.2, 98.1)
- added V27_36: AUTO_VIA, VIA_MATRIX, F.Cu at (153.2, 100.6)
- added V27_38: AUTO_VIA, VIA_MATRIX, F.Cu at (153.2, 105.7)
- added V27_44: AUTO_VIA, VIA_MATRIX, F.Cu at (153.2, 121.0)
- added V28_16: AUTO_VIA, VIA_MATRIX, F.Cu at (155.8, 49.8)
- added V28_17: AUTO_VIA, VIA_MATRIX, F.Cu at (155.8, 52.4)
- added V28_18: AUTO_VIA, VIA_MATRIX, F.Cu at (155.8, 54.9)
- added V28_20: AUTO_VIA, VIA_MATRIX, F.Cu at (155.8, 60.0)
- added V28_21: AUTO_VIA, VIA_MATRIX, F.Cu at (155.8, 62.5)
- added V28_22: AUTO_VIA, VIA_MATRIX, F.Cu at (155.8, 65.1)
- added V28_23: AUTO_VIA, VIA_MATRIX, F.Cu at (155.8, 67.6)
- added V28_32: AUTO_VIA, VIA_MATRIX, F.Cu at (155.8, 90.5)
- added V28_33: AUTO_VIA, VIA_MATRIX, F.Cu at (155.8, 93.0)
- added V28_35: AUTO_VIA, VIA_MATRIX, F.Cu at (155.8, 98.1)
- added V28_38: AUTO_VIA, VIA_MATRIX, F.Cu at (155.8, 105.7)
- added V28_39: AUTO_VIA, VIA_MATRIX, F.Cu at (155.8, 108.3)
- added V28_44: AUTO_VIA, VIA_MATRIX, F.Cu at (155.8, 121.0)
- added V29_17: AUTO_VIA, VIA_MATRIX, F.Cu at (158.3, 52.4)
- added V29_18: AUTO_VIA, VIA_MATRIX, F.Cu at (158.3, 54.9)
- added V29_20: AUTO_VIA, VIA_MATRIX, F.Cu at (158.3, 60.0)
- added V29_38: AUTO_VIA, VIA_MATRIX, F.Cu at (158.3, 105.7)
- added V2_11: AUTO_VIA, VIA_MATRIX, F.Cu at (89.7, 37.1)
- added V2_12: AUTO_VIA, VIA_MATRIX, F.Cu at (89.7, 39.7)
- added V2_13: AUTO_VIA, VIA_MATRIX, F.Cu at (89.7, 42.2)
- added V2_14: AUTO_VIA, VIA_MATRIX, F.Cu at (89.7, 44.8)
- added V2_15: AUTO_VIA, VIA_MATRIX, F.Cu at (89.7, 47.3)
- added V2_16: AUTO_VIA, VIA_MATRIX, F.Cu at (89.7, 49.8)
- added V2_17: AUTO_VIA, VIA_MATRIX, F.Cu at (89.7, 52.4)
- added V2_18: AUTO_VIA, VIA_MATRIX, F.Cu at (89.7, 54.9)
- added V2_19: AUTO_VIA, VIA_MATRIX, F.Cu at (89.7, 57.5)
- added V2_20: AUTO_VIA, VIA_MATRIX, F.Cu at (89.7, 60.0)
- added V2_41: AUTO_VIA, VIA_MATRIX, F.Cu at (89.7, 113.3)
- added V2_42: AUTO_VIA, VIA_MATRIX, F.Cu at (89.7, 115.9)
- added V2_43: AUTO_VIA, VIA_MATRIX, F.Cu at (89.7, 118.4)
- added V2_44: AUTO_VIA, VIA_MATRIX, F.Cu at (89.7, 121.0)
- added V2_45: AUTO_VIA, VIA_MATRIX, F.Cu at (89.7, 123.5)
- added V2_46: AUTO_VIA, VIA_MATRIX, F.Cu at (89.7, 126.0)
- added V2_47: AUTO_VIA, VIA_MATRIX, F.Cu at (89.7, 128.6)
- added V2_48: AUTO_VIA, VIA_MATRIX, F.Cu at (89.7, 131.1)
- added V2_49: AUTO_VIA, VIA_MATRIX, F.Cu at (89.7, 133.7)
- added V30_11: AUTO_VIA, VIA_MATRIX, F.Cu at (160.8, 37.1)
- added V30_12: AUTO_VIA, VIA_MATRIX, F.Cu at (160.8, 39.7)
- added V30_13: AUTO_VIA, VIA_MATRIX, F.Cu at (160.8, 42.2)
- added V30_14: AUTO_VIA, VIA_MATRIX, F.Cu at (160.8, 44.8)
- added V30_15: AUTO_VIA, VIA_MATRIX, F.Cu at (160.8, 47.3)
- added V30_16: AUTO_VIA, VIA_MATRIX, F.Cu at (160.8, 49.8)
- added V30_17: AUTO_VIA, VIA_MATRIX, F.Cu at (160.8, 52.4)
- added V30_18: AUTO_VIA, VIA_MATRIX, F.Cu at (160.8, 54.9)
- added V30_19: AUTO_VIA, VIA_MATRIX, F.Cu at (160.8, 57.5)
- added V30_22: AUTO_VIA, VIA_MATRIX, F.Cu at (160.8, 65.1)
- added V30_23: AUTO_VIA, VIA_MATRIX, F.Cu at (160.4, 67.8)
- added V30_42: AUTO_VIA, VIA_MATRIX, F.Cu at (160.8, 115.9)
- added V30_43: AUTO_VIA, VIA_MATRIX, F.Cu at (160.8, 118.4)
- added V31_11: AUTO_VIA, VIA_MATRIX, F.Cu at (163.4, 37.1)
- added V31_12: AUTO_VIA, VIA_MATRIX, F.Cu at (163.4, 39.7)
- added V31_13: AUTO_VIA, VIA_MATRIX, F.Cu at (163.4, 42.2)
- added V31_14: AUTO_VIA, VIA_MATRIX, F.Cu at (163.4, 44.8)
- added V31_15: AUTO_VIA, VIA_MATRIX, F.Cu at (163.4, 47.3)
- added V31_16: AUTO_VIA, VIA_MATRIX, F.Cu at (163.4, 49.8)
- added V31_17: AUTO_VIA, VIA_MATRIX, F.Cu at (163.4, 52.4)
- added V31_18: AUTO_VIA, VIA_MATRIX, F.Cu at (163.4, 54.9)
- added V31_19: AUTO_VIA, VIA_MATRIX, F.Cu at (163.4, 57.5)
- added V31_26: AUTO_VIA, VIA_MATRIX, F.Cu at (163.4, 75.2)
- added V32_11: AUTO_VIA, VIA_MATRIX, F.Cu at (165.9, 37.1)
- added V32_12: AUTO_VIA, VIA_MATRIX, F.Cu at (165.9, 39.7)
- added V32_13: AUTO_VIA, VIA_MATRIX, F.Cu at (165.9, 42.2)
- added V32_14: AUTO_VIA, VIA_MATRIX, F.Cu at (165.9, 44.8)
- added V32_15: AUTO_VIA, VIA_MATRIX, F.Cu at (165.9, 47.3)
- added V32_16: AUTO_VIA, VIA_MATRIX, F.Cu at (165.9, 49.8)
- added V32_17: AUTO_VIA, VIA_MATRIX, F.Cu at (165.9, 52.4)
- added V32_18: AUTO_VIA, VIA_MATRIX, F.Cu at (165.9, 54.9)
- added V32_19: AUTO_VIA, VIA_MATRIX, F.Cu at (165.9, 57.5)
- added V32_20: AUTO_VIA, VIA_MATRIX, F.Cu at (165.9, 60.0)
- added V32_21: AUTO_VIA, VIA_MATRIX, F.Cu at (165.9, 62.5)
- added V33_11: AUTO_VIA, VIA_MATRIX, F.Cu at (168.5, 37.1)
- added V33_12: AUTO_VIA, VIA_MATRIX, F.Cu at (168.5, 39.7)
- added V33_13: AUTO_VIA, VIA_MATRIX, F.Cu at (168.5, 42.2)
- added V33_14: AUTO_VIA, VIA_MATRIX, F.Cu at (168.5, 44.8)
- added V33_15: AUTO_VIA, VIA_MATRIX, F.Cu at (168.5, 47.3)
- added V33_16: AUTO_VIA, VIA_MATRIX, F.Cu at (168.5, 49.8)
- added V33_17: AUTO_VIA, VIA_MATRIX, F.Cu at (168.5, 52.4)
- added V33_18: AUTO_VIA, VIA_MATRIX, F.Cu at (168.5, 54.9)
- added V33_19: AUTO_VIA, VIA_MATRIX, F.Cu at (168.5, 57.5)
- added V33_20: AUTO_VIA, VIA_MATRIX, F.Cu at (168.5, 60.0)
- added V33_21: AUTO_VIA, VIA_MATRIX, F.Cu at (168.5, 62.5)
- added V33_35: AUTO_VIA, VIA_MATRIX, F.Cu at (168.5, 98.1)
- added V33_36: AUTO_VIA, VIA_MATRIX, F.Cu at (168.5, 100.6)
- added V33_37: AUTO_VIA, VIA_MATRIX, F.Cu at (168.5, 103.2)
- added V33_38: AUTO_VIA, VIA_MATRIX, F.Cu at (168.5, 105.7)
- added V33_39: AUTO_VIA, VIA_MATRIX, F.Cu at (168.5, 108.3)
- added V33_44: AUTO_VIA, VIA_MATRIX, F.Cu at (168.5, 121.0)
- added V34_11: AUTO_VIA, VIA_MATRIX, F.Cu at (171.0, 37.1)
- added V34_12: AUTO_VIA, VIA_MATRIX, F.Cu at (171.0, 39.7)
- added V34_13: AUTO_VIA, VIA_MATRIX, F.Cu at (171.0, 42.2)
- added V34_14: AUTO_VIA, VIA_MATRIX, F.Cu at (171.0, 44.8)
- added V34_15: AUTO_VIA, VIA_MATRIX, F.Cu at (171.0, 47.3)
- added V34_16: AUTO_VIA, VIA_MATRIX, F.Cu at (171.0, 49.8)
- added V34_17: AUTO_VIA, VIA_MATRIX, F.Cu at (171.0, 52.4)
- added V34_18: AUTO_VIA, VIA_MATRIX, F.Cu at (171.0, 54.9)
- added V34_19: AUTO_VIA, VIA_MATRIX, F.Cu at (171.0, 57.5)
- added V34_20: AUTO_VIA, VIA_MATRIX, F.Cu at (171.0, 60.0)
- added V34_23: AUTO_VIA, VIA_MATRIX, F.Cu at (171.0, 67.6)
- added V34_35: AUTO_VIA, VIA_MATRIX, F.Cu at (171.0, 98.1)
- added V34_36: AUTO_VIA, VIA_MATRIX, F.Cu at (171.0, 100.6)
- added V34_37: AUTO_VIA, VIA_MATRIX, F.Cu at (171.0, 103.2)
- added V34_38: AUTO_VIA, VIA_MATRIX, F.Cu at (171.0, 105.7)
- added V35_11: AUTO_VIA, VIA_MATRIX, F.Cu at (173.5, 37.1)
- added V35_12: AUTO_VIA, VIA_MATRIX, F.Cu at (173.5, 39.7)
- added V35_13: AUTO_VIA, VIA_MATRIX, F.Cu at (173.5, 42.2)
- added V35_14: AUTO_VIA, VIA_MATRIX, F.Cu at (173.5, 44.8)
- added V35_15: AUTO_VIA, VIA_MATRIX, F.Cu at (173.5, 47.3)
- added V35_16: AUTO_VIA, VIA_MATRIX, F.Cu at (173.5, 49.8)
- added V35_17: AUTO_VIA, VIA_MATRIX, F.Cu at (173.5, 52.4)
- added V35_18: AUTO_VIA, VIA_MATRIX, F.Cu at (173.5, 54.9)
- added V35_19: AUTO_VIA, VIA_MATRIX, F.Cu at (173.5, 57.5)
- added V35_20: AUTO_VIA, VIA_MATRIX, F.Cu at (173.5, 60.0)
- added V35_25: AUTO_VIA, VIA_MATRIX, F.Cu at (173.5, 72.7)
- added V36_11: AUTO_VIA, VIA_MATRIX, F.Cu at (176.1, 37.1)
- added V36_12: AUTO_VIA, VIA_MATRIX, F.Cu at (176.1, 39.7)
- added V36_13: AUTO_VIA, VIA_MATRIX, F.Cu at (176.1, 42.2)
- added V36_14: AUTO_VIA, VIA_MATRIX, F.Cu at (176.1, 44.8)
- added V36_15: AUTO_VIA, VIA_MATRIX, F.Cu at (176.1, 47.3)
- added V36_16: AUTO_VIA, VIA_MATRIX, F.Cu at (176.1, 49.8)
- added V36_17: AUTO_VIA, VIA_MATRIX, F.Cu at (176.1, 52.4)
- added V36_18: AUTO_VIA, VIA_MATRIX, F.Cu at (176.1, 54.9)
- added V36_19: AUTO_VIA, VIA_MATRIX, F.Cu at (176.1, 57.5)
- added V36_20: AUTO_VIA, VIA_MATRIX, F.Cu at (176.1, 60.0)
- added V36_32: AUTO_VIA, VIA_MATRIX, F.Cu at (176.1, 90.5)
- added V36_33: AUTO_VIA, VIA_MATRIX, F.Cu at (173.2, 95.2)
- added V36_33: AUTO_VIA, VIA_MATRIX, F.Cu at (176.1, 93.0)
- added V36_45: AUTO_VIA, VIA_MATRIX, F.Cu at (176.1, 123.5)
- added V36_46: AUTO_VIA, VIA_MATRIX, F.Cu at (176.1, 126.0)
- added V36_47: AUTO_VIA, VIA_MATRIX, F.Cu at (171.5, 123.4)
- added V36_47: AUTO_VIA, VIA_MATRIX, F.Cu at (164.4, 133.4)
- added V36_47: AUTO_VIA, VIA_MATRIX, F.Cu at (164.8, 129.6)
- added V36_47: AUTO_VIA, VIA_MATRIX, F.Cu at (176.1, 128.6)
- added V37_11: AUTO_VIA, VIA_MATRIX, F.Cu at (178.6, 37.1)
- added V37_12: AUTO_VIA, VIA_MATRIX, F.Cu at (178.6, 39.7)
- added V37_13: AUTO_VIA, VIA_MATRIX, F.Cu at (178.6, 42.2)
- added V37_14: AUTO_VIA, VIA_MATRIX, F.Cu at (178.6, 44.8)
- added V37_15: AUTO_VIA, VIA_MATRIX, F.Cu at (178.6, 47.3)
- added V37_16: AUTO_VIA, VIA_MATRIX, F.Cu at (178.6, 49.8)
- added V37_17: AUTO_VIA, VIA_MATRIX, F.Cu at (178.6, 52.4)
- added V37_18: AUTO_VIA, VIA_MATRIX, F.Cu at (178.6, 54.9)
- added V37_19: AUTO_VIA, VIA_MATRIX, F.Cu at (178.6, 57.5)
- added V37_20: AUTO_VIA, VIA_MATRIX, F.Cu at (178.6, 60.0)
- added V37_45: AUTO_VIA, VIA_MATRIX, F.Cu at (178.6, 123.5)
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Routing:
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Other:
- net class Default: trace_width 0.2 -> 0.25

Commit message: first submission to pcbway
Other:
- board size 430.6 x 213.9 mm -> 100 x 100 mm
